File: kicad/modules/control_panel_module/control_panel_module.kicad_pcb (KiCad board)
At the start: 2 copper layers, 75 x 28 mm, 18 parts, among them J1 Screw_Terminal_01x06, J2 Screw_Terminal_01x06, U1 ULN2004A

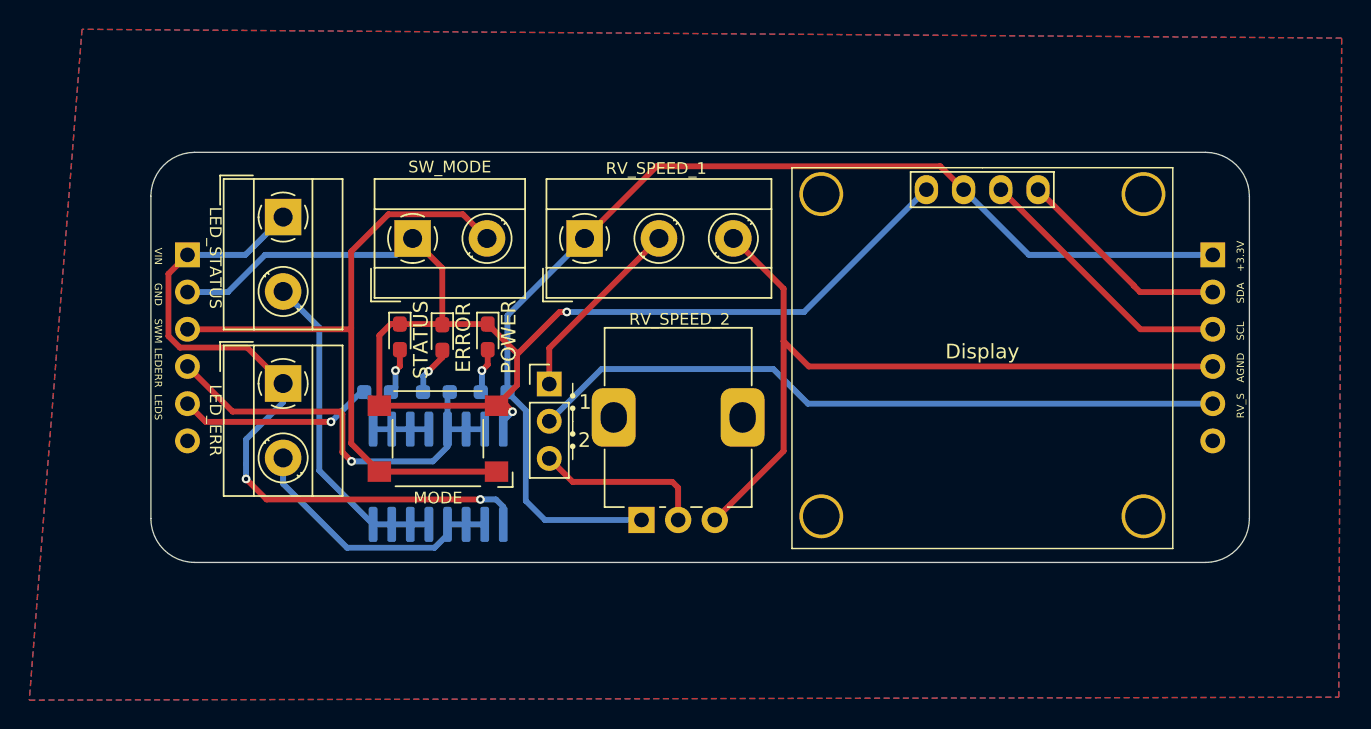
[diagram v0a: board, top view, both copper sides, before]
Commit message: dots for orientation
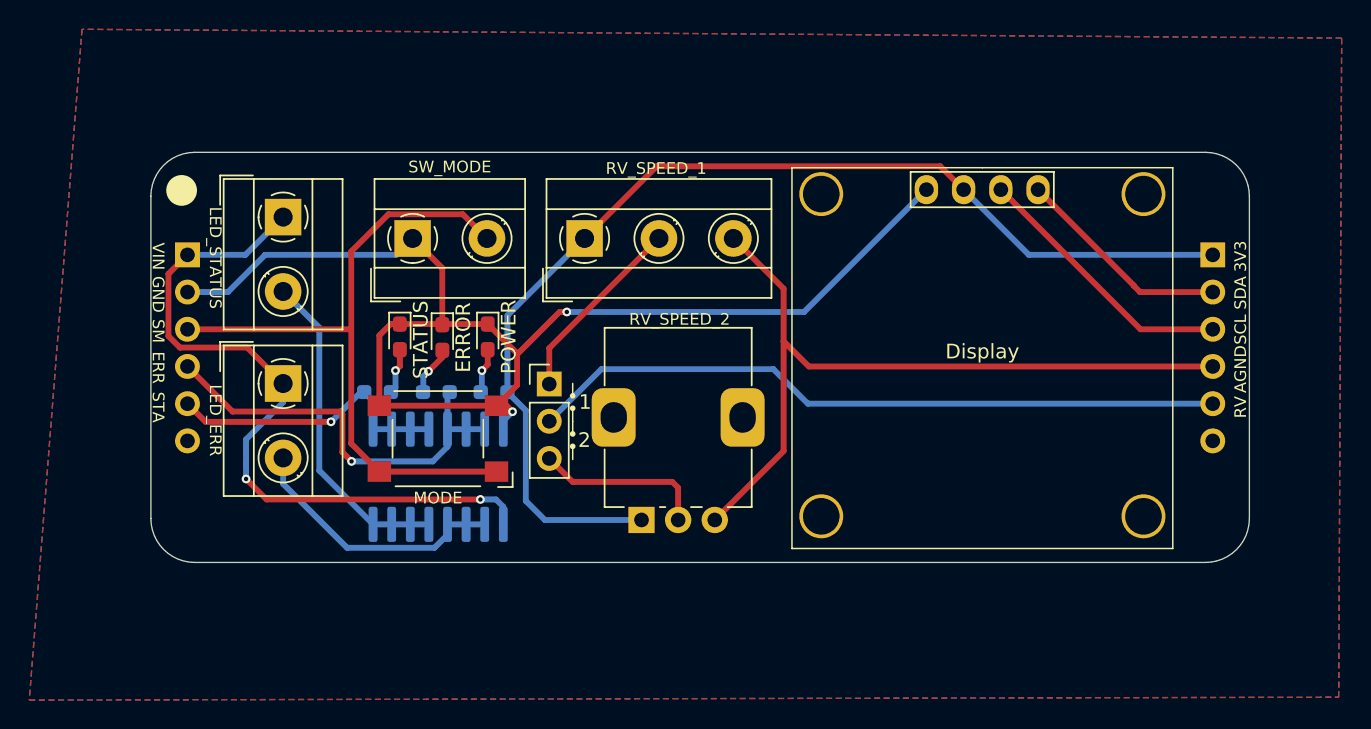
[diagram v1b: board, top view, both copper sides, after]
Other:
- board text added: "3V3"
- board text added: "ERR"
- board text added: "RV"
- board text added: "SM"
- board text added: "STA"
- board text removed: "+3.3V"
- board text removed: "LEDERR"
- board text removed: "LEDS"
- board text removed: "RV_S"
- board text removed: "SWM"
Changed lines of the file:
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@@
+	)
+	(gr_circle
+		(center 65.6 52.6)
+		(end 66.6 52.6)
+		(stroke
+			(width 0.1)
+			(type solid)
+		)
+		(fill solid)
+		(layer "F.SilkS")
 	)
 	(gr_circle
@@
 		)
 	)
-	(gr_text "LEDS\n"
-		(at 64 67.4 -90)
-		(layer "F.SilkS")
-		(effects
-			(font
-				(size 0.5 0.5)
-				(thickness 0.07)
-			)
-		)
-	)
-	(gr_text "SWM"
-		(at 64 62.2 -90)
-		(layer "F.SilkS")
-		(effects
-			(font
-				(size 0.5 0.5)
-				(thickness 0.07)
+	(gr_text "STA"
+		(at 64 67.4 270)
+		(layer "F.SilkS")
+		(effects
+			(font
+				(size 0.8 0.8)
+				(thickness 0.1)
+			)
+		)
+	)
+	(gr_text "SM"
+		(at 64 62.2 270)
+		(layer "F.SilkS")
+		(effects
+			(font
+				(size 0.8 0.8)
+				(thickness 0.1)
 			)
 		)
@@
 	)
 	(gr_text "SCL"
-		(at 137.9 62.2 90)
-		(layer "F.SilkS")
-		(effects
-			(font
-				(size 0.5 0.5)
-				(thickness 0.07)
+		(at 137.9 62.1 90)
+		(layer "F.SilkS")
+		(effects
+			(font
+				(size 0.8 0.8)
+				(thickness 0.1)
 			)
 		)
@@
 	)
 	(gr_text "GND"
-		(at 64 59.7 -90)
-		(layer "F.SilkS")
-		(effects
-			(font
-				(size 0.5 0.5)
-				(thickness 0.07)
-			)
-		)
-	)
-	(gr_text "RV_S"
-		(at 137.9 67.3 90)
-		(layer "F.SilkS")
-		(effects
-			(font
-				(size 0.5 0.5)
-				(thickness 0.07)
+		(at 64 59.7 270)
+		(layer "F.SilkS")
+		(effects
+			(font
+				(size 0.8 0.8)
+				(thickness 0.1)
+			)
+		)
+	)
+	(gr_text "RV"
+		(at 137.9 67.4 90)
+		(layer "F.SilkS")
+		(effects
+			(font
+				(size 0.8 0.8)
+				(thickness 0.1)
 			)
 		)
 	)
 	(gr_text "VIN"
-		(at 64 57.1 -90)
-		(layer "F.SilkS")
-		(effects
-			(font
-				(size 0.5 0.5)
-				(thickness 0.07)
+		(at 64 57.1 270)
+		(layer "F.SilkS")
+		(effects
+			(font
+				(size 0.8 0.8)
+				(thickness 0.1)
 			)
 		)
 	)
 	(gr_text "AGND"
-		(at 137.9 64.7 90)
-		(layer "F.SilkS")
-		(effects
-			(font
-				(size 0.5 0.5)
-				(thickness 0.07)
+		(at 137.9 64.8 90)
+		(layer "F.SilkS")
+		(effects
+			(font
+				(size 0.8 0.8)
+				(thickness 0.1)
 			)
 		)
@@
 		(effects
 			(font
-				(size 0.5 0.5)
-				(thickness 0.07)
-			)
-		)
-	)
-	(gr_text "LEDERR"
-		(at 64 64.7 -90)
-		(layer "F.SilkS")
-		(effects
-			(font
-				(size 0.5 0.5)
-				(thickness 0.07)
-			)
-		)
-	)
-	(gr_text "+3.3V"
+				(size 0.8 0.8)
+				(thickness 0.1)
+			)
+		)
+	)
+	(gr_text "ERR"
+		(at 64 64.7 270)
+		(layer "F.SilkS")
+		(effects
+			(font
+				(size 0.8 0.8)
+				(thickness 0.1)
+			)
+		)
+	)
+	(gr_text "3V3"
 		(at 137.9 57.1 90)
 		(layer "F.SilkS")
 		(effects
 			(font
-				(size 0.5 0.5)
-				(thickness 0.07)
-			)
-		)
+				(size 0.8 0.8)
+				(thickness 0.1)
+			)
+		)

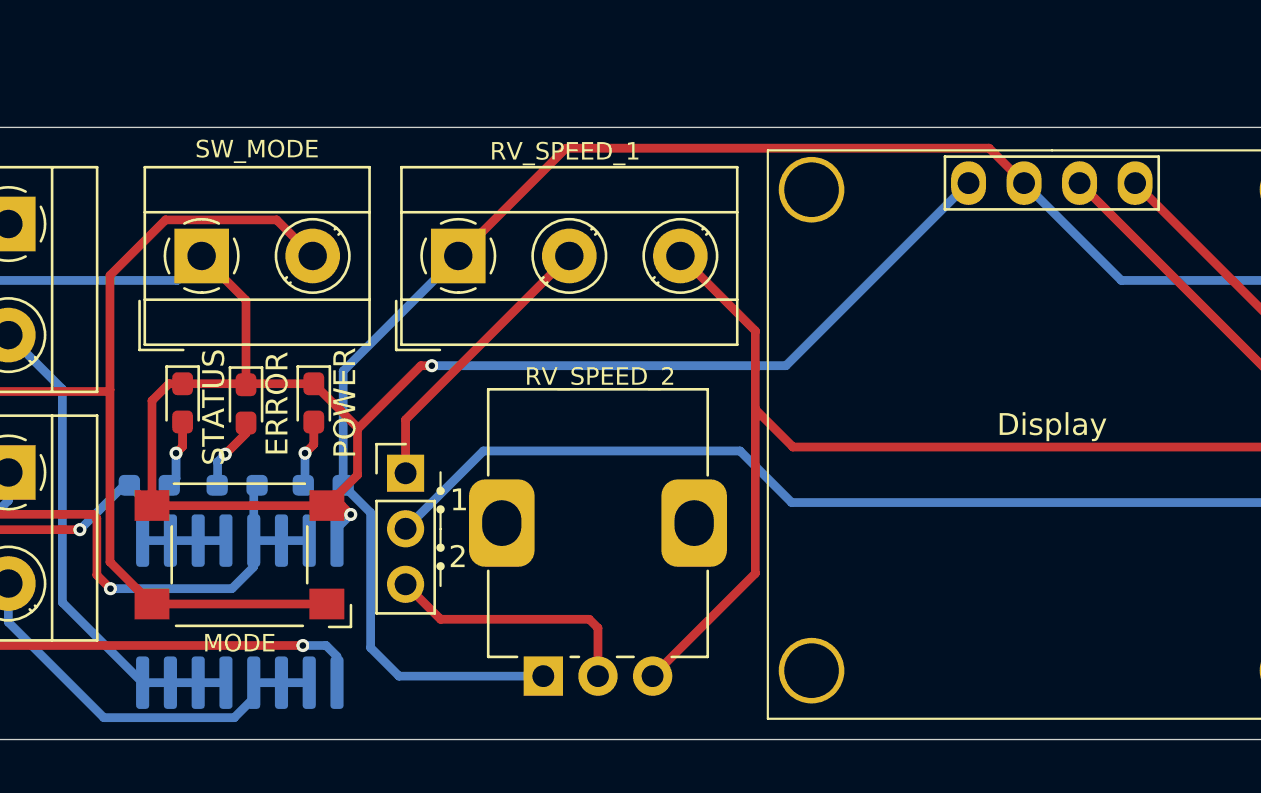
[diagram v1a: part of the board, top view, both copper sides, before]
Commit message: LED footprint update
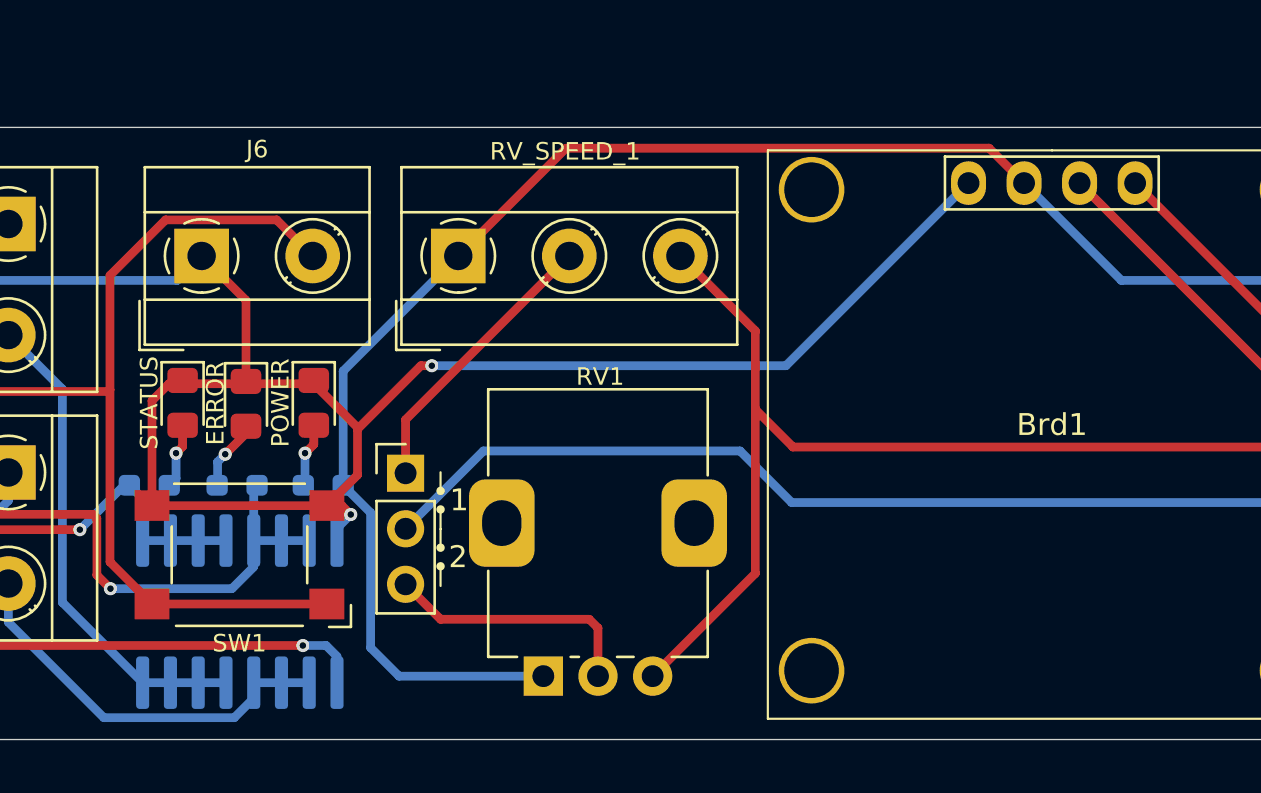
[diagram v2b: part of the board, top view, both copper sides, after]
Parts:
- ERROR, POWER, STATUS: footprint LED_SMD:LED_0603_1608Metric_Pad1.05x0.95mm_HandSolder -> LED_SMD:LED_0805_2012Metric_Pad1.15x1.40mm_HandSolder
- J1, J2: value Screw_Terminal_01x06 -> 1x6 2.54
- J3: renamed from LED_STATUS_OFFBOARD1; value Screw_Terminal_01x02 -> 1x2 5.08
- J4: renamed from LED_ERR_OFFBOARD1; value Screw_Terminal_01x02 -> 1x3 5.08
- J5: renamed from RV_SPEED1; value Screw_Terminal_01x03 -> 1x3 5.08
- J6: renamed from SW_MODE; value Screw_Terminal_01x02 -> 1x2 5.08
- JP1: value Jumper_3_Bridged12 -> 1x3 2.54
- renumbered Display to Brd1, RV_SPEED_2 to RV1, MODE to SW1
